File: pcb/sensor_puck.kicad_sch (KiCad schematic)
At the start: 61 parts, among them J1 DISP LEFT, J2 DISP RIGHT, J3 USB_C_Receptacle_USB2.0_16P, J5 Generic, SW1 RST, SW2 BOOT, U1 ESP32-S3-MINI-1U, U2 LIS3MDL, U3 LSM6DSOXTR, U4 STC31-C-R3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

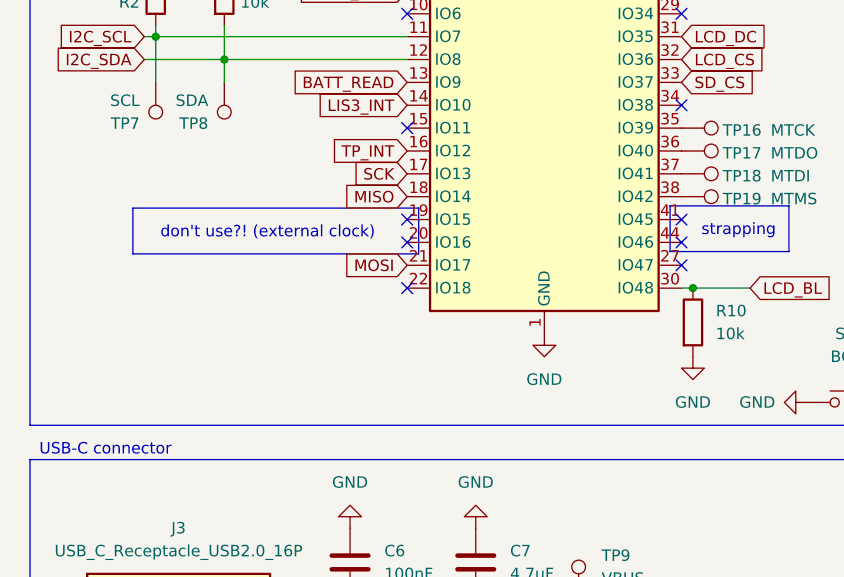
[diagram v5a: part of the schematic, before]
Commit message: feat(pcb): enable monitoring VBUS voltage level
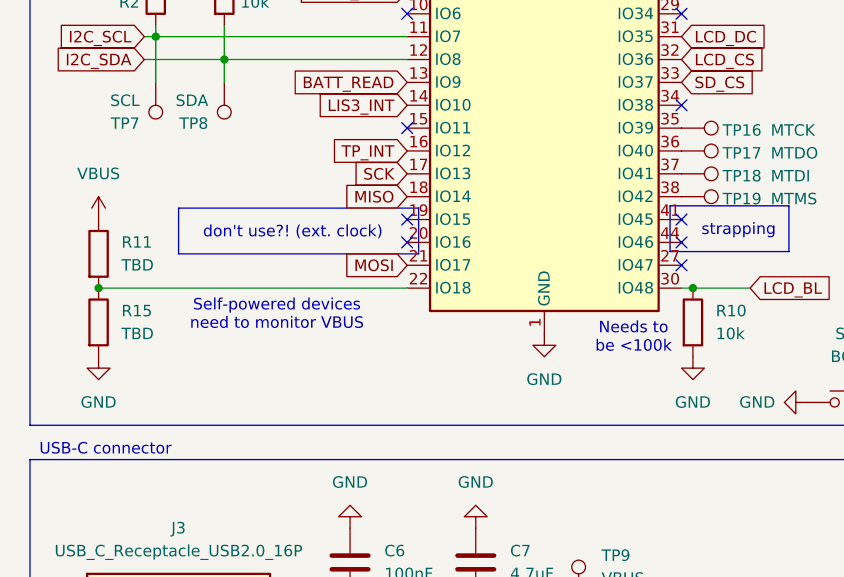
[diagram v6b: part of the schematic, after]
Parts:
- added R11, R15: TBD, symbol Device:R
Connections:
- net GND: now also R15.2
- net VBUS: now also R11.1
- net at U1.22 (IO18): now also R11.2, R15.1
- no-connect marks 20 -> 19
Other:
- note added: "Needs to be <100k"
- note added: "Self-powered devices need to monitor VBUS"
- note added: "don't use?! (ext. clock)"
- note removed: "don't use?! (external clock)"

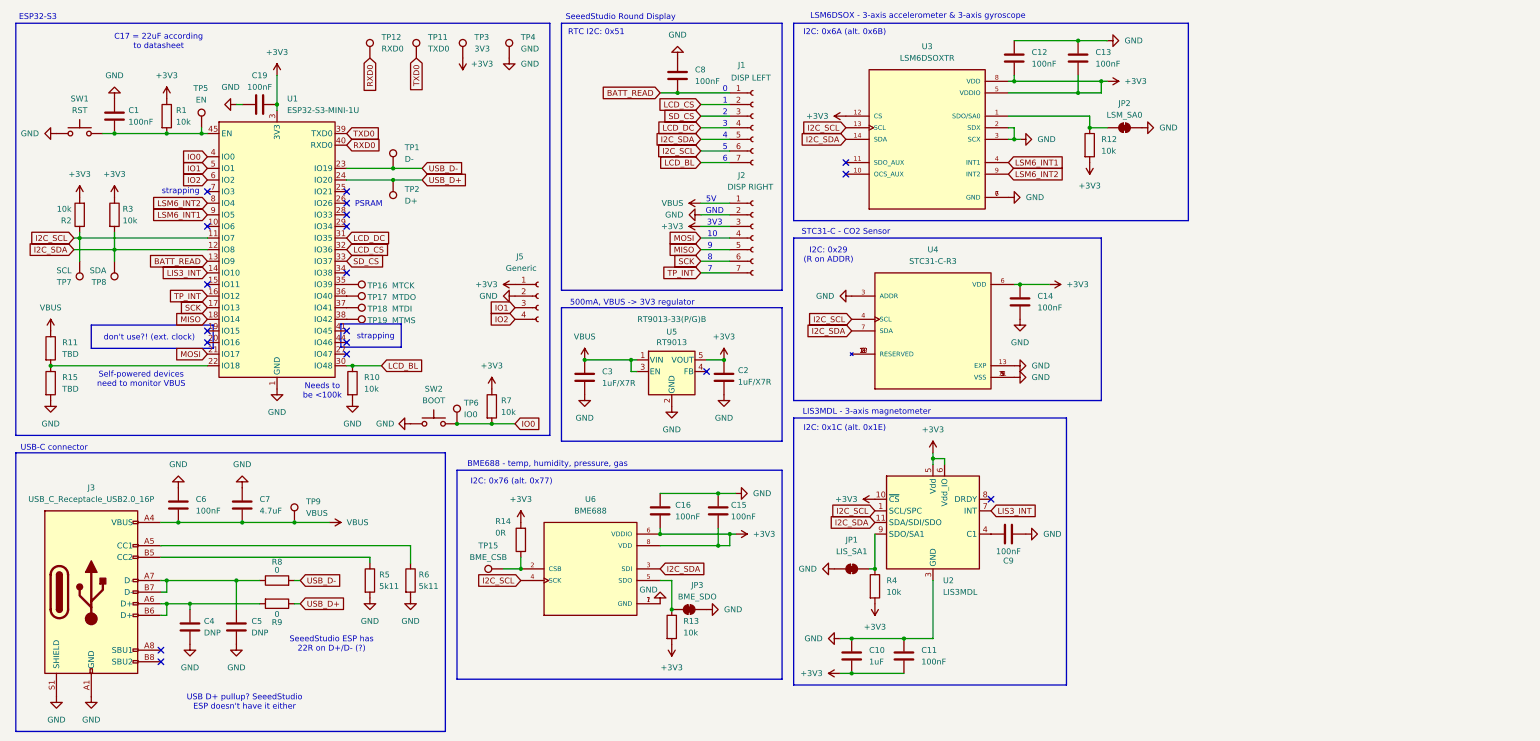
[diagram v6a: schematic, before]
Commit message: chore(schematic): use LIS2MDL instead of LIS3MDL
Since the LIS3MDL is now NRND (approaching EOL), we should use a
different magnetometer. The LIS2MDL seems to be a close replacement
here, also offering 3-axis magnetic sensing.
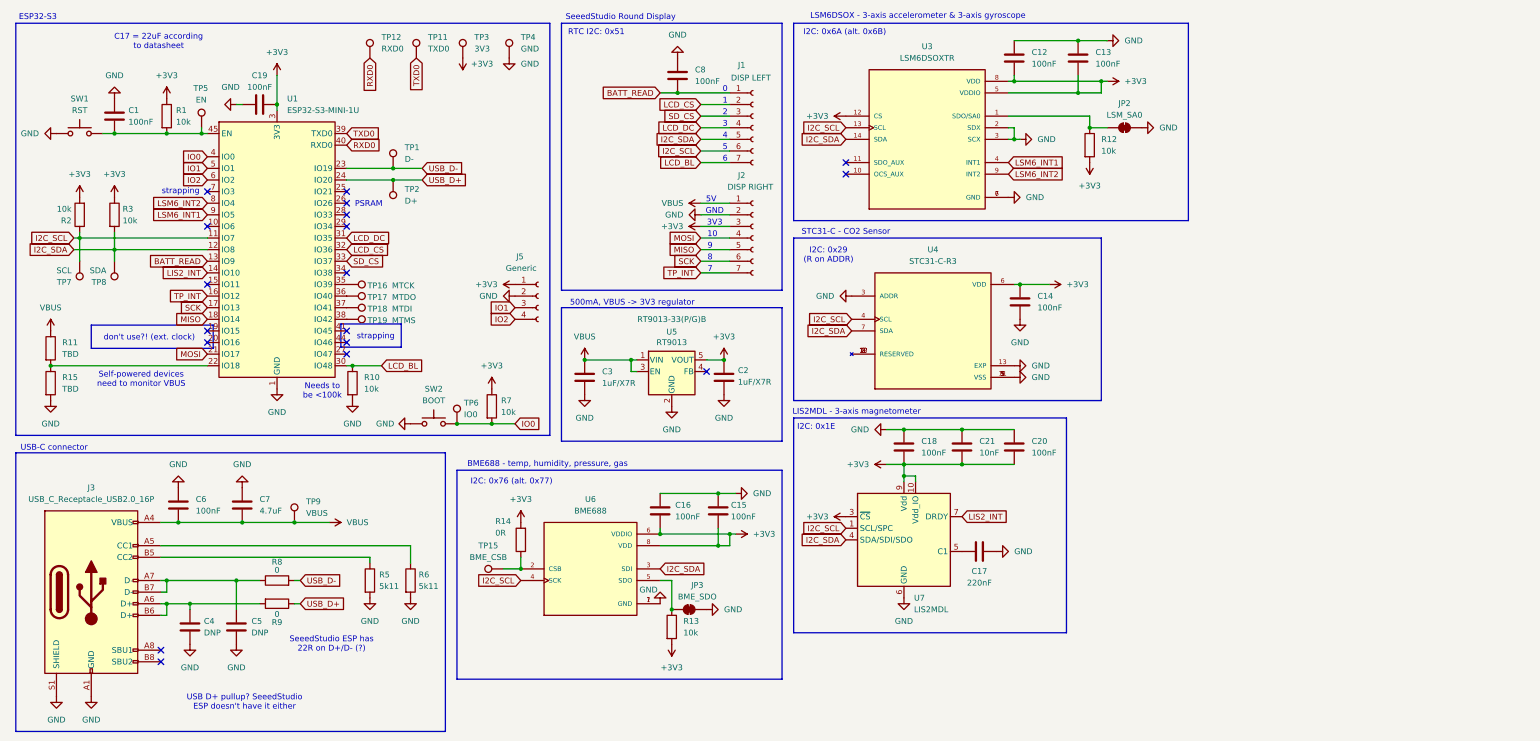
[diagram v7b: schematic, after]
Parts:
- removed C10: 1uF, Capacitor_SMD:C_0805_2012Metric, symbol Device:C
- removed C11, C9: 100nF, Capacitor_SMD:C_0805_2012Metric, symbol Device:C
- removed JP1: LIS_SA1, Jumper:SolderJumper-2_P1.3mm_Bridged_RoundedPad1.0x1.5mm, symbol Jumper:SolderJumper_2_Bridged
- removed R4: 10k, Resistor_SMD:R_0805_2012Metric, symbol Device:R
- removed U2: LIS3MDL, Package_LGA:LGA-12_2x2mm_P0.5mm, symbol Sensor_Magnetic:LIS3MDL
- added C17: 220nF, symbol Device:C
- added C18, C20: 100nF, symbol Device:C
- added C21: 10nF, symbol Device:C
- added U7: LIS2MDL, Package_LGA:LGA-12_2x2mm_P0.5mm, symbol Sensor_Magnetic:LIS2MDL
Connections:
- net +3V3: now also C18.1, C20.1, C21.1, U7.10 (Vdd_IO), U7.3 (~{CS}), U7.9 (Vdd)
- net GND: now also C17.2, C18.2, C20.2, C21.2, U7.6 (GND), U7.8 (GND)
- net I2C_SCL: now also U7.1 (SCL/SPC)
- net I2C_SDA: now also U7.4 (SDA/SDI/SDO)
- net LIS3_INT renamed LIS2_INT
- net LIS2_INT: now also U7.7 (DRDY)
- new net: C17.1, U7.5 (C1)
- no-connect marks 19 -> 18
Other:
- note added: "I2C: 0x1E"
- note added: "LIS2MDL - 3-axis magnetometer"
- note removed: "I2C: 0x1C (alt. 0x1E)"
- note removed: "LIS3MDL - 3-axis magnetometer"

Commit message: feat(schematic): add ST25DVxxK dynamic NFC tag
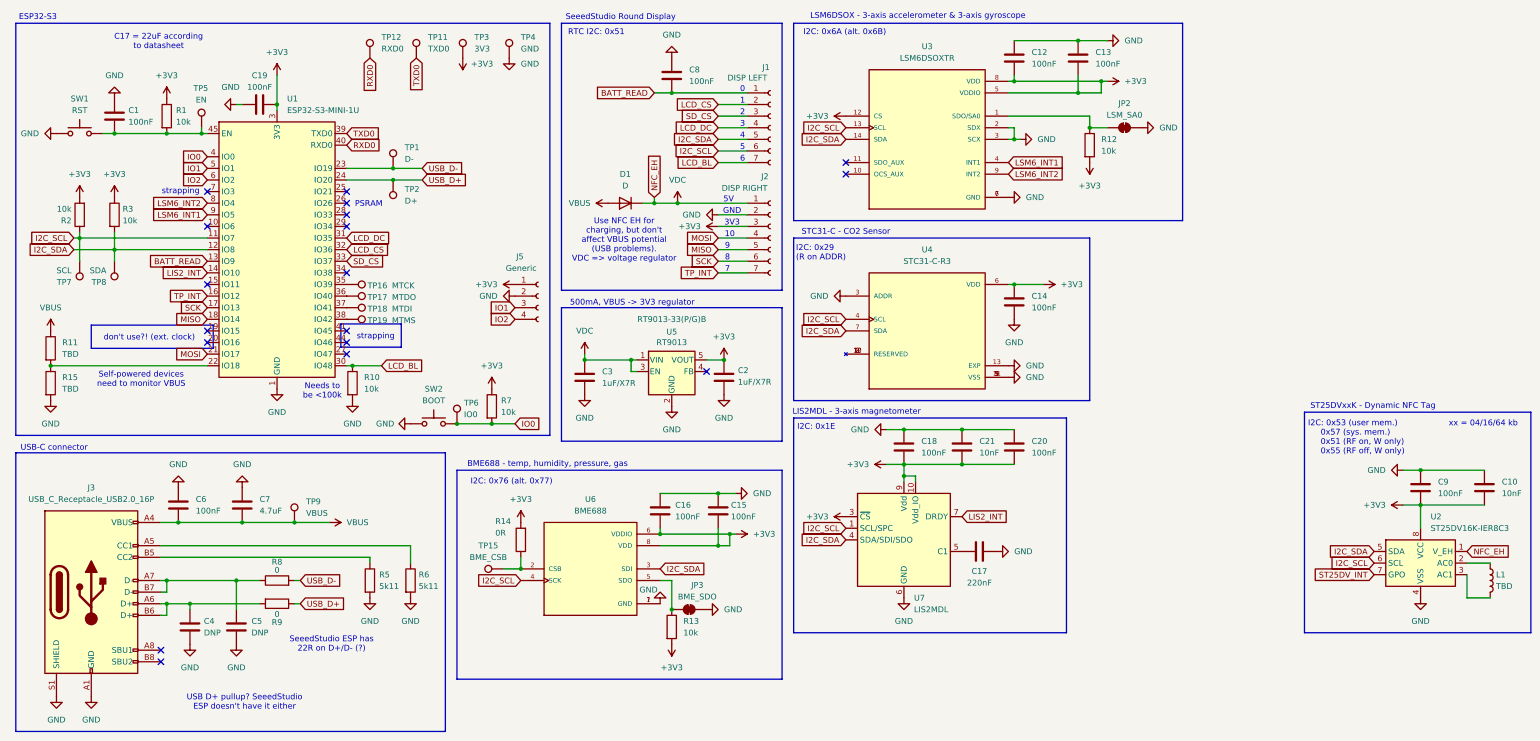
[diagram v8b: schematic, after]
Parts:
- added C10: 10nF, symbol Device:C
- added C9: 100nF, symbol Device:C
- added D1: D, symbol Device:D
- added L1: TBD, symbol Device:L
- added U2: ST25DV16K-IER8C3, Package_DFN_QFN:DFN-8-1EP_3x2mm_P0.5mm_EP1.36x1.46mm, symbol RF_NFC:ST25DV16K-IER8C3
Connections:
- net +3V3: now also C10.2, C9.2, U2.8 (VCC)
- net GND: now also C10.1, C9.1, U2.4 (VSS)
- net I2C_SCL: now also U2.6 (SCL)
- net I2C_SDA: now also U2.5 (SDA)
- net VBUS: now also D1.2 (A); no longer C3.2, J2.1 (Pin_1), U5.1 (VIN), U5.3 (EN)
- new net: L1.1, U2.2 (AC0)
- new net: L1.2, U2.3 (AC1)
- new net ST25DV_INT: U2.7 (GPO)
- new net VDC: C3.2, D1.1 (K), J2.1 (Pin_1), U2.1 (V_EH), U5.1 (VIN), U5.3 (EN)
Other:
- note added: "I2C: 0x53 (user mem.) 0x57 (sys. mem.) 0x51 (RF on, W only) 0x55 (RF off, W only)"
- note added: "ST25DVxxK - Dynamic NFC Tag"
- note added: "Use NFC EH for charging, but don't affect VBUS potential (USB problems). VDC => voltage regulator"
- note added: "xx = 04/16/64 kb"
- moved on the sheet: C14, C8, J1, J2, U4
